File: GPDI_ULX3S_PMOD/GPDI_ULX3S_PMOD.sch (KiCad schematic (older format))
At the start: 53 parts, among them J2 PMOD, P1 HDMI-D, U1 RN5RK501A, U2 PCA9306

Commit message: Renaming - routing new GPDI PMOD
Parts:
- removed C10: 220nF, Capacitor_SMD:C_0603_1608Metric_Pad1.05x0.95mm_HandSolder, symbol Device:C
- removed JP2, JP3, JP4, JP5, JP6: JUMP, Jumper:SolderJumper-2_P1.3mm_Bridged_RoundedPad1.0x1.5mm, symbol Jumper:SolderJumper_2_Bridged
- added D3: BZT52C3V6S-7-F, Diode_SMD:D_SOD-323, symbol antena:D_Zener_Small
- added JP2: SJO, Jumper:SolderJumper-2_P1.3mm_Open_RoundedPad1.0x1.5mm, symbol Jumper:SolderJumper_2_Open
- added R28: 510, Resistor_SMD:R_0402_1005Metric, symbol Device:R
- added R29: 4.7k, Resistor_SMD:R_0402_1005Metric, symbol Device:R
- C1, C13, C2, C3, C4, C5, C6, C7, C8, C9: footprint Capacitor_SMD:C_0603_1608Metric_Pad1.05x0.95mm_HandSolder -> Capacitor_SMD:C_0402_1005Metric
- C11, C12: Mouser (none) -> https://hr.mouser.com/ProductDetail/AVX/F911A476MAAAJ6?qs=%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
- D1: Mouser (none) -> https://hr.mouser.com/ProductDetail/ON-Semiconductor/MBR052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
- JP1: value JUMP -> SJB
- L1: footprint Inductor_SMD:L_1210_3225Metric_Pad1.42x2.65mm_HandSolder -> Inductor_SMD:L_1210_3225Metric; Mouser (none) -> https://hr.mouser.com/ProductDetail/Taiyo-Yuden/CBC3225T101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
- R1, R10, R11, R12, R13, R14, R15, R16, R17, R18, R19, R2, R20, R21, R22, R23, R24, R25, R26, R27, R3, R4, R5, R6, R7, R8, R9: footprint Resistor_SMD:R_0603_1608Metric_Pad1.05x0.95mm_HandSolder -> Resistor_SMD:R_0402_1005Metric
- U1: footprint Package_TO_SOT_SMD:SOT-23-5_HandSoldering -> Package_TO_SOT_SMD:SOT-23-5; symbol HDMI-rescue:RN5RK501A -> GPDI_ULX3S_PMOD-rescue:RN5RK501A-HDMI-rescue; Field7 None -> (none); Mouser (none) -> https://hr.mouser.com/ProductDetail/Ricoh-Electronic-Device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
- U2: footprint Package_SO:SSOP-8_2.95x2.8mm_P0.65mm -> Package_SO:VSSOP-8_2.3x2mm_P0.5mm; Mouser (none) -> https://hr.mouser.com/ProductDetail/NXP-Semiconductors/PCA9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
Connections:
- wire segments 163 -> 168
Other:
- note added: "3.6V zener\nLowering 5V from \nmonitor to 3.6V"
- note added: "Default: Off"
- note added: "GP13 ETH+\nGN13 ETH- over 510 ohm resistor\nGP12 CLK+\nGN12 CLK-\nGP11 D2+\nGN11 D2-\nGP10 D1+\nGN10 D1-\nGP9 D0+\nGN9 D0-\nGP8 SDA over i2c chip\nGN8 SCL over i2c chip\nGP7 CEC over 510 ohm resistor\nGN7 onboard LED"
- note removed: "GP13 ETH+\nGN13 ETH-\nGP12 CLK+\nGN12 CLK-\nGP11 D2+\nGN11 D2-\nGP10 D1+\nGN10 D1-\nGP9 D0+\nGN9 D0-\nGP8 SDA over i2c chip\nGN8 SCL over i2c chip\nGP7 CEC over 510 ohm resistor\nGN7 onboard LED"
- moved on the sheet: C13, R10, R11, R12, R13, R14, R15, R16, R17, R18, R19, R20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

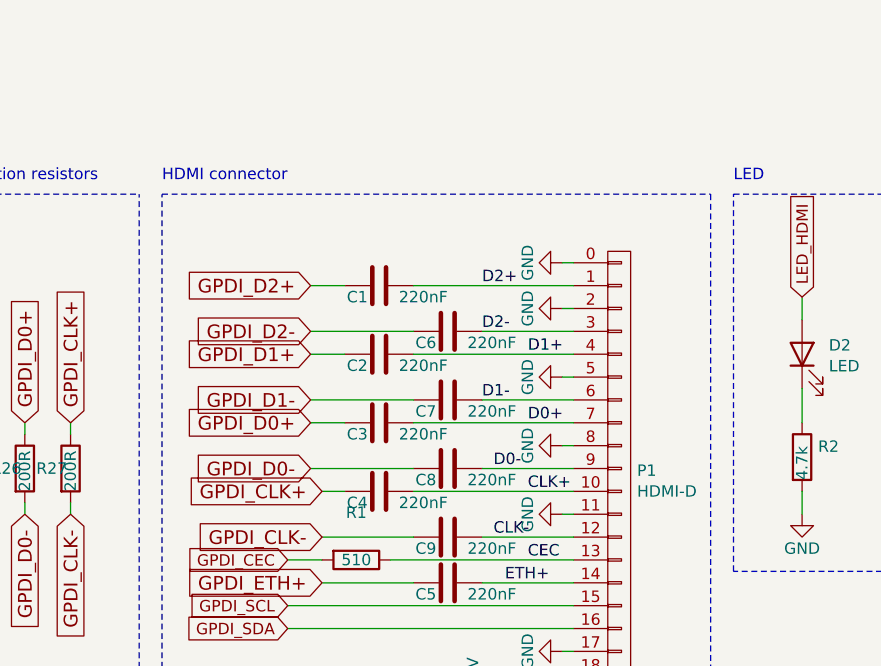
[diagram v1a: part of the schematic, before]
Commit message: Changing GPDI connector as used on ULX3S
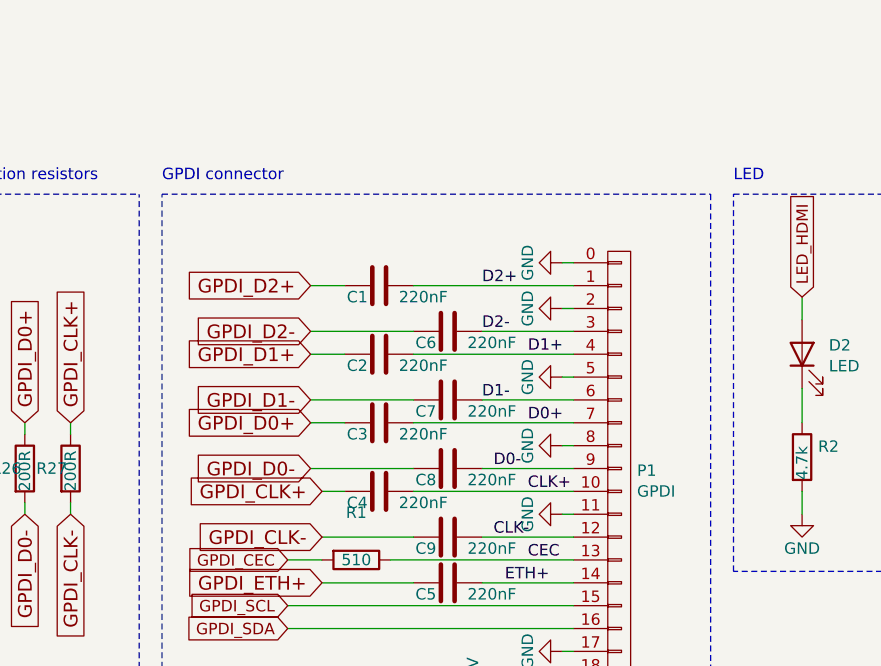
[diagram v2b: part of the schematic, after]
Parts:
- P1: value HDMI-D -> GPDI; footprint HDMI:HDMI-D -> GPDI:CONN-10029449-111RLF
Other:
- note added: "GPDI connector"
- note removed: "HDMI connector"
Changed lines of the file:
@@
 P 3950 4800
 F 0 "P1" H 4028 4841 50  0000 L CNN
-F 1 "HDMI-D" H 4028 4750 50  0000 L CNN
-F 2 "HDMI:HDMI-D" H 3950 4800 60  0001 C CNN
+F 1 "GPDI" H 4028 4750 50  0000 L CNN
+F 2 "GPDI:CONN-10029449-111RLF" H 3950 4800 60  0001 C CNN
 F 3 "" H 3950 4800 60  0000 C CNN
 	1    3950 4800
@@
 	1950 6000 1950 3550
 Text Notes 1950 3500 0    50   ~ 0
-HDMI connector
+GPDI connector
 Wire Notes Line
 	5200 3550 7850 3550

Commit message: Adding GPDI version 1.5
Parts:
- removed R24, R25, R26, R27: 200R, Resistor_SMD:R_0402_1005Metric, symbol antena:R
- D3: symbol antena:D_Zener_Small -> GPDI_ULX3S_PMOD-rescue:D_Zener_Small-antena-GPDI_ULX3S_PMOD-rescue
- J2: value PMOD -> CONN
- R10, R11, R12, R13, R14, R15, R16, R17, R18, R19, R20, R21, R22, R23, R8, R9: symbol antena:R -> GPDI_ULX3S_PMOD-rescue:R-antena-GPDI_ULX3S_PMOD-rescue
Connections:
- wire segments 168 -> 160
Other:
- note added: "5V DC/DC"
- note added: "GPDI_Extension"
- note removed: "HDMI needs 5V"
- note removed: "PMOD"
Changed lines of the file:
@@
 encoding utf-8
 Sheet 1 1
-Title "GPDI PMOD for ULX3S"
+Title "GPDI extension for ULX3S"
 Date "2020-09-08"
 Rev "1.4"
@@
 P 8850 4350
 F 0 "J2" H 8900 4967 50  0000 C CNN
-F 1 "PMOD" H 8900 4876 50  0000 C CNN
+F 1 "CONN" H 8900 4876 50  0000 C CNN
 F 2 "Connector_PinHeader_2.54mm:PinHeader_2x09_P2.54mm_Horizontal" H 8850 4350 50  0001 C CNN
 F 3 "~" H 8850 4350 50  0001 C CNN
@@
 CLK-
 $Comp
-L antena:R R11
+L GPDI_ULX3S_PMOD-rescue:R-antena-GPDI_ULX3S_PMOD-rescue R11
 U 1 1 5E2CBDF3
 P 4500 1800
@@
 $EndComp
 $Comp
-L antena:R R12
+L GPDI_ULX3S_PMOD-rescue:R-antena-GPDI_ULX3S_PMOD-rescue R12
 U 1 1 5E2CC017
 P 4700 1800
@@
 $EndComp
 $Comp
-L antena:R R15
+L GPDI_ULX3S_PMOD-rescue:R-antena-GPDI_ULX3S_PMOD-rescue R15
 U 1 1 5E2CC065
 P 4900 1800
@@
 $EndComp
 $Comp
-L antena:R R16
+L GPDI_ULX3S_PMOD-rescue:R-antena-GPDI_ULX3S_PMOD-rescue R16
 U 1 1 5E2CC0C5
 P 5100 1800
@@
 $EndComp
 $Comp
-L antena:R R19
+L GPDI_ULX3S_PMOD-rescue:R-antena-GPDI_ULX3S_PMOD-rescue R19
 U 1 1 5E2CC11B
 P 5300 1800
@@
 $EndComp
 $Comp
-L antena:R R20
+L GPDI_ULX3S_PMOD-rescue:R-antena-GPDI_ULX3S_PMOD-rescue R20
 U 1 1 5E2CC16F
 P 5500 1800
@@
 $EndComp
 $Comp
-L antena:R R8
+L GPDI_ULX3S_PMOD-rescue:R-antena-GPDI_ULX3S_PMOD-rescue R8
 U 1 1 5E2CC1C5
 P 4300 1800
@@
 $EndComp
 $Comp
-L antena:R R23
+L GPDI_ULX3S_PMOD-rescue:R-antena-GPDI_ULX3S_PMOD-rescue R23
 U 1 1 5E2CC21D
 P 5700 1800
@@
 $EndComp
 $Comp
-L antena:R R17
+L GPDI_ULX3S_PMOD-rescue:R-antena-GPDI_ULX3S_PMOD-rescue R17
 U 1 1 5E34419C
 P 7100 1350
@@
 $EndComp
 $Comp
-L antena:R R18
+L GPDI_ULX3S_PMOD-rescue:R-antena-GPDI_ULX3S_PMOD-rescue R18
 U 1 1 5E3441A2
 P 7100 1800
@@
 GPDI_D2+
 $Comp
-L antena:R R13
+L GPDI_ULX3S_PMOD-rescue:R-antena-GPDI_ULX3S_PMOD-rescue R13
 U 1 1 5E34947B
 P 6600 1350
@@
 $EndComp
 $Comp
-L antena:R R14
+L GPDI_ULX3S_PMOD-rescue:R-antena-GPDI_ULX3S_PMOD-rescue R14
 U 1 1 5E349481
 P 6600 1800
@@
 GPDI_D1+
 $Comp
-L antena:R R9
+L GPDI_ULX3S_PMOD-rescue:R-antena-GPDI_ULX3S_PMOD-rescue R9
 U 1 1 5E34949B
 P 6150 1350
@@
 $EndComp
 $Comp
-L antena:R R10
+L GPDI_ULX3S_PMOD-rescue:R-antena-GPDI_ULX3S_PMOD-rescue R10
 U 1 1 5E3494A1
 P 6150 1800
@@
 	5200 3550 7850 3550
 Text Notes 5200 3500 0    50   ~ 0
-HDMI needs 5V
+5V DC/DC
 Wire Notes Line
 	8000 3550 9800 3550
@@
 	8000 3550 8000 4900
 Text Notes 8000 3500 0    50   ~ 0
-PMOD
+GPDI_Extension
 Wire Notes Line
 	7900 650  7900 3000
@@
 Wire Wire Line
 	7550 4500 7550 4600
-Text GLabel 850  4550 1    60   Input ~ 0
-GPDI_D2+
-Text GLabel 850  4950 3    60   Input ~ 0
-GPDI_D2-
-Text GLabel 1100 4550 1    60   Input ~ 0
-GPDI_D1+
-Text GLabel 1100 4950 3    60   Input ~ 0
-GPDI_D1-
-Text GLabel 1350 4550 1    60   Input ~ 0
-GPDI_D0+
-Text GLabel 1350 4950 3    60   Input ~ 0
-GPDI_D0-
-Text GLabel 1550 4950 3    60   Input ~ 0
-GPDI_CLK-
-Text GLabel 1550 4550 1    60   Input ~ 0
-GPDI_CLK+
-$Comp
-L antena:R R24
-U 1 1 5E9188DF
-P 850 4750
-F 0 "R24" H 700 4750 50  0000 L CNN
-F 1 "200R" V 850 4650 50  0000 L CNN
-F 2 "Resistor_SMD:R_0402_1005Metric" V 780 4750 50  0001 C CNN
-F 3 "~" H 850 4750 50  0001 C CNN
-	1    850  4750
-	1    0    0    -1
-$EndComp
-$Comp
-L antena:R R25
-U 1 1 5E918E84
-P 1100 4750
-F 0 "R25" H 950 4750 50  0000 L CNN
-F 1 "200R" V 1100 4650 50  0000 L CNN
-F 2 "Resistor_SMD:R_0402_1005Metric" V 1030 4750 50  0001 C CNN
-F 3 "~" H 1100 4750 50  0001 C CNN
-	1    1100 4750
-	1    0    0    -1
-$EndComp
-$Comp
-L antena:R R26
-U 1 1 5E918F06
-P 1350 4750
-F 0 "R26" H 1200 4750 50  0000 L CNN
-F 1 "200R" V 1350 4650 50  0000 L CNN
-F 2 "Resistor_SMD:R_0402_1005Metric" V 1280 4750 50  0001 C CNN
-F 3 "~" H 1350 4750 50  0001 C CNN
-	1    1350 4750
-	1    0    0    -1
-$EndComp
-$Comp
-L antena:R R27
-U 1 1 5E918F8A
-P 1550 4750
-F 0 "R27" H 1400 4750 50  0000 L CNN
-F 1 "200R" V 1550 4650 50  0000 L CNN
-F 2 "Resistor_SMD:R_0402_1005Metric" V 1480 4750 50  0001 C CNN
-F 3 "~" H 1550 4750 50  0001 C CNN
-	1    1550 4750
-	1    0    0    -1
-$EndComp
-Wire Wire Line
-	850  4550 850  4600
-Wire Wire Line
-	1100 4550 1100 4600
-Wire Wire Line
-	1350 4550 1350 4600
-Wire Wire Line
-	1550 4550 1550 4600
-Wire Wire Line
-	850  4900 850  4950
-Wire Wire Line
-	1100 4900 1100 4950
-Wire Wire Line
-	1350 4900 1350 4950
-Wire Wire Line
-	1550 4900 1550 4950
 $Comp
 L power:GND #PWR0115
@@
 $EndComp
 $Comp
-L antena:R R22
+L GPDI_ULX3S_PMOD-rescue:R-antena-GPDI_ULX3S_PMOD-rescue R22
 U 1 1 5E316F15
 P 7550 1800
@@
 $EndComp
 $Comp
-L antena:R R21
+L GPDI_ULX3S_PMOD-rescue:R-antena-GPDI_ULX3S_PMOD-rescue R21
 U 1 1 5E316EA7
 P 7550 1350
@@
 	7550 1950 7550 2050
 $Comp
-L antena:D_Zener_Small D3
+L GPDI_ULX3S_PMOD-rescue:D_Zener_Small-antena-GPDI_ULX3S_PMOD-rescue D3
 U 1 1 5F5539A7
 P 10300 4300
